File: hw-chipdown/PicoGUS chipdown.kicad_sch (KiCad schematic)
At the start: 65 parts, among them J1 Bus_ISA_8bit, J10 Conn_01x02_Pin, J2 DEBUG, J3 IRQDMA_JP, J4 UART_TX, J5 USB_A - joy, J7 3.5mm TRS, J8 Wavetable, J9 3.5mm TRS, Q1 AO3401A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

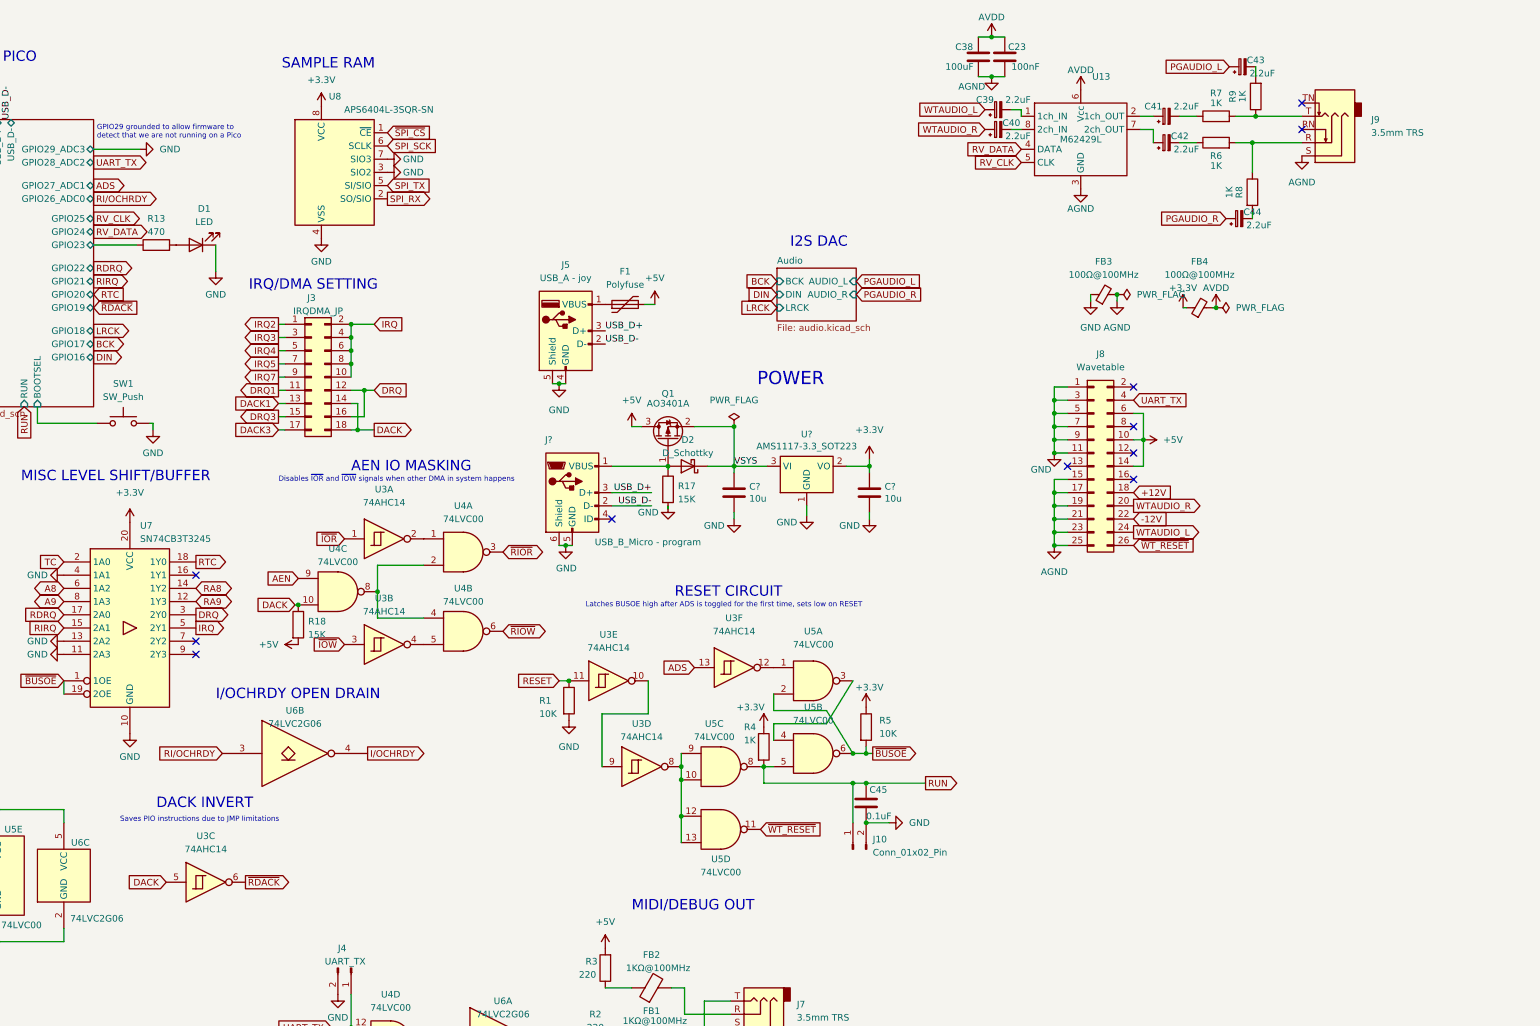
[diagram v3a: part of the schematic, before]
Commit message: Add S/PDIF optical output to board
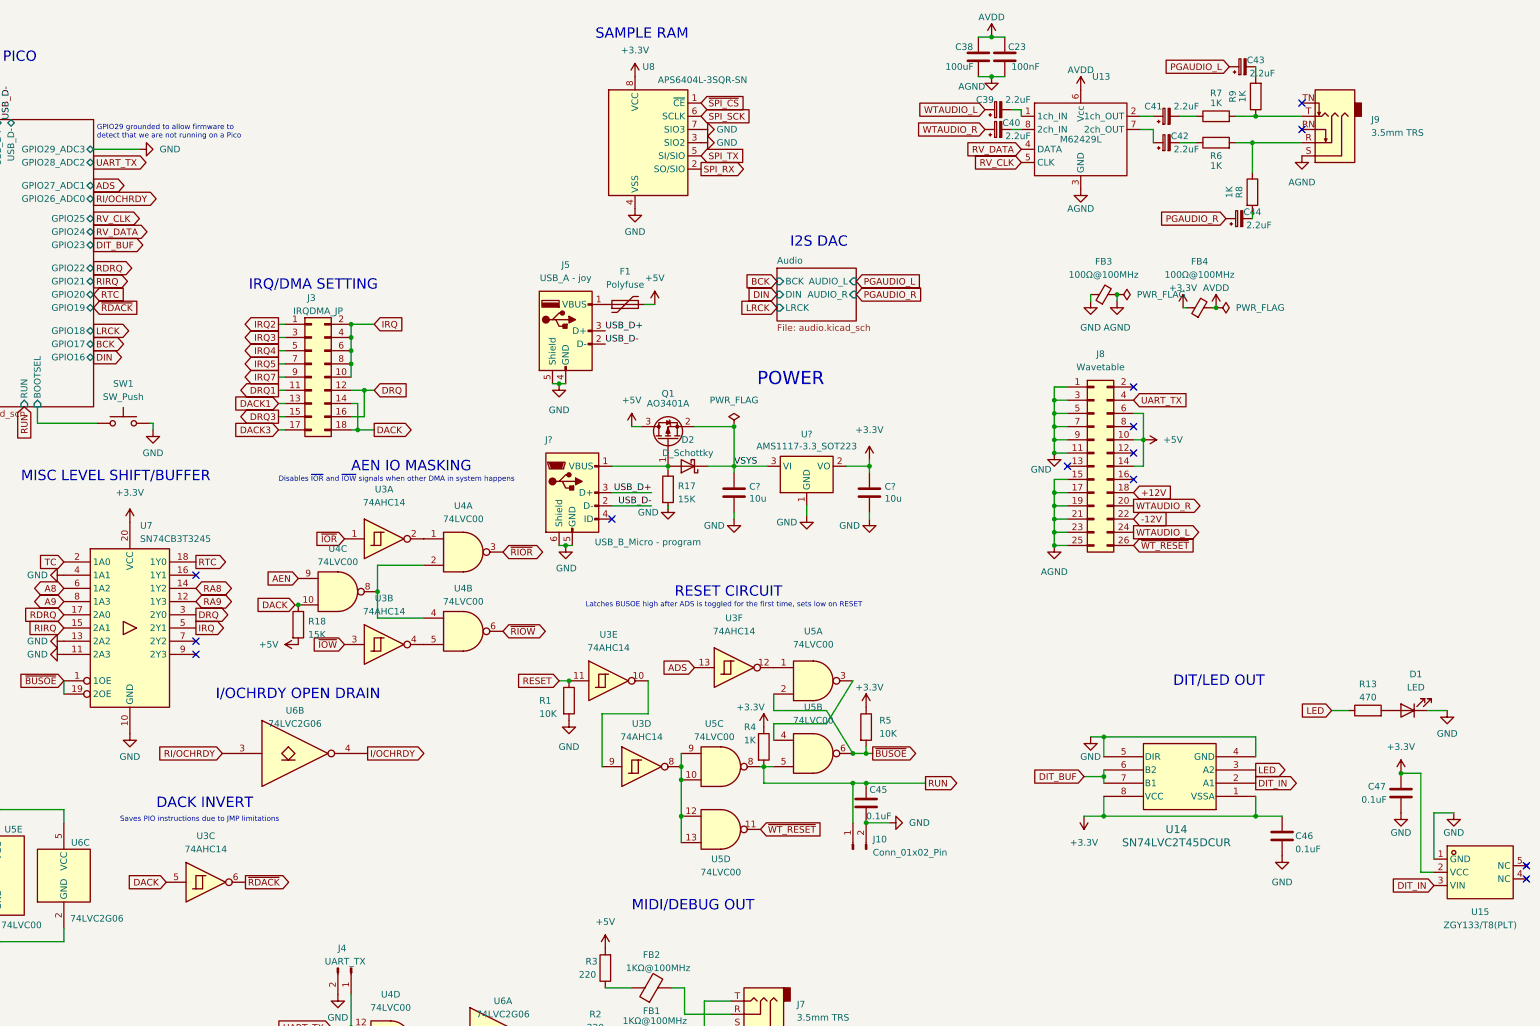
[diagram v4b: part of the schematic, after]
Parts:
- added C46, C47: 0.1uF, Capacitor_SMD:C_0402_1005Metric, symbol Device:C
- added U14: SN74LVC2T45DCUR, PiGUS library:DCU8, symbol PiGUS library:SN74LVC2T45DCUR
- added U15: ZGY133/T8(PLT), PiGUS library:OPTO-TH_ZGY133-T8-PLT, symbol PiGUS library:OPTO-TH_ZGY133-T8-PLT
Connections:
- net +3V3: now also C46.1, C47.1, U14.1 (VSSA), U14.8 (VCC), U15.2 (VCC)
- net GND: now also C46.2, C47.2, U14.4 (GND), U14.5 (DIR), U15.1 (GND)
- net RP2040/GPIO23 renamed LED
- net LED: now also U14.3 (A2)
- new net DIT_BUF: U14.6 (B2), U14.7 (B1)
- new net DIT_IN: U14.2 (A1), U15.3 (VIN)
- no-connect marks 33 -> 35
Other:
- note added: "DIT/LED OUT"
- moved on the sheet: U8

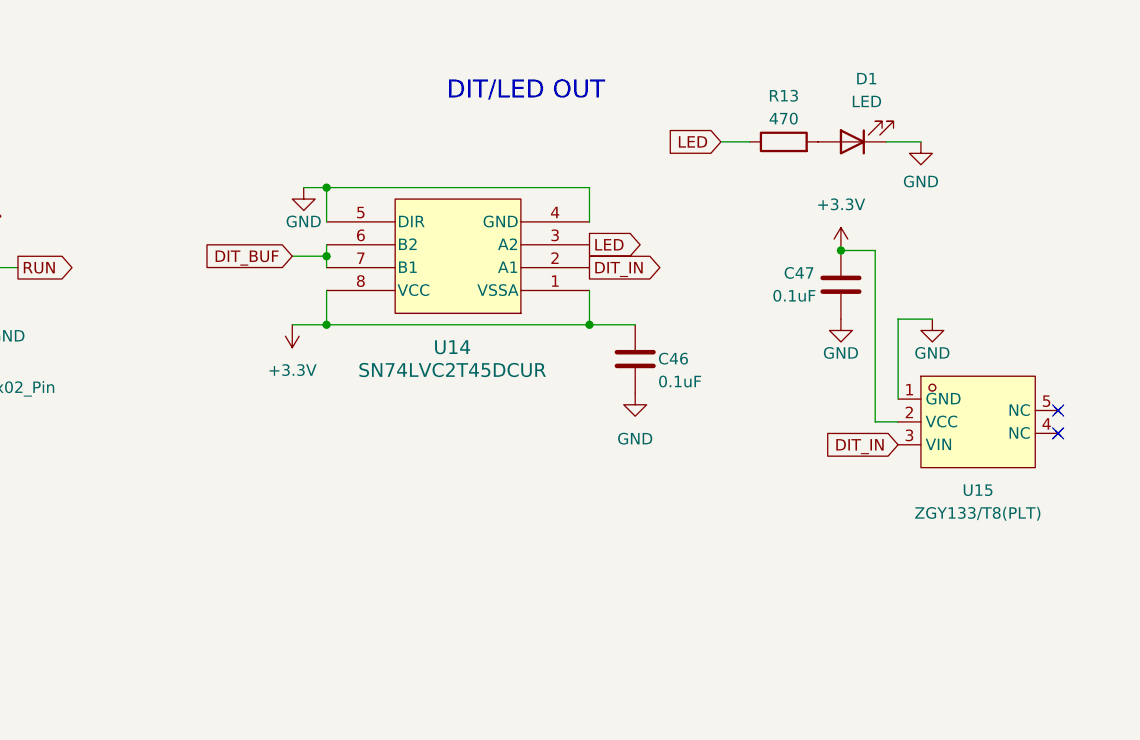
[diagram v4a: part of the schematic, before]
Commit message: use SN74LVC2G34 instead
Cheaper and more available
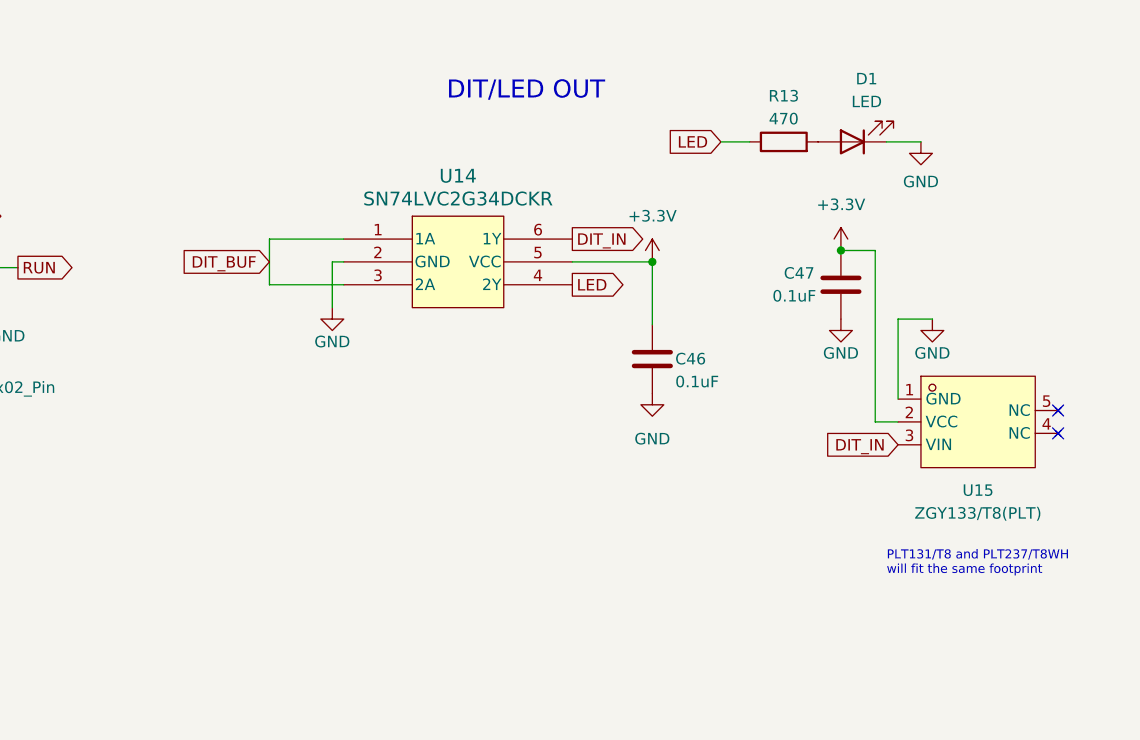
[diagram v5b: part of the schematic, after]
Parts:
- removed U14: SN74LVC2T45DCUR, PiGUS library:DCU8, symbol PiGUS library:SN74LVC2T45DCUR
- added U14: SN74LVC2G34DCKR, Package_TO_SOT_SMD:SOT-363_SC-70-6, symbol PiGUS library:SN74LVC2G34DCKR
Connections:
- net +3V3: now also U14.5 (VCC)
- net DIT_BUF: now also U14.1 (1A), U14.3 (2A)
- net DIT_IN: now also U14.6 (1Y)
- net GND: now also U14.2 (GND)
- net LED: now also U14.4 (2Y)
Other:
- note added: "PLT131/T8 and PLT237/T8WH will fit the same footprint"
- moved on the sheet: C46
